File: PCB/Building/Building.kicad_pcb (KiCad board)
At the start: 2 copper layers, 57.7 x 111.5 mm, 34 parts, among them IC1 HT16K33-28SOP, IC2 HT16K33-28SOP, IC3 HT16K33-28SOP, J1 Conn_01x05, U1 OSL60362_IX, U2 OSL60362_IX, U3 OSL60362_IX, U4 OSL60362_IX, U5 OSL60362_IX, U6 OSL60362_IX

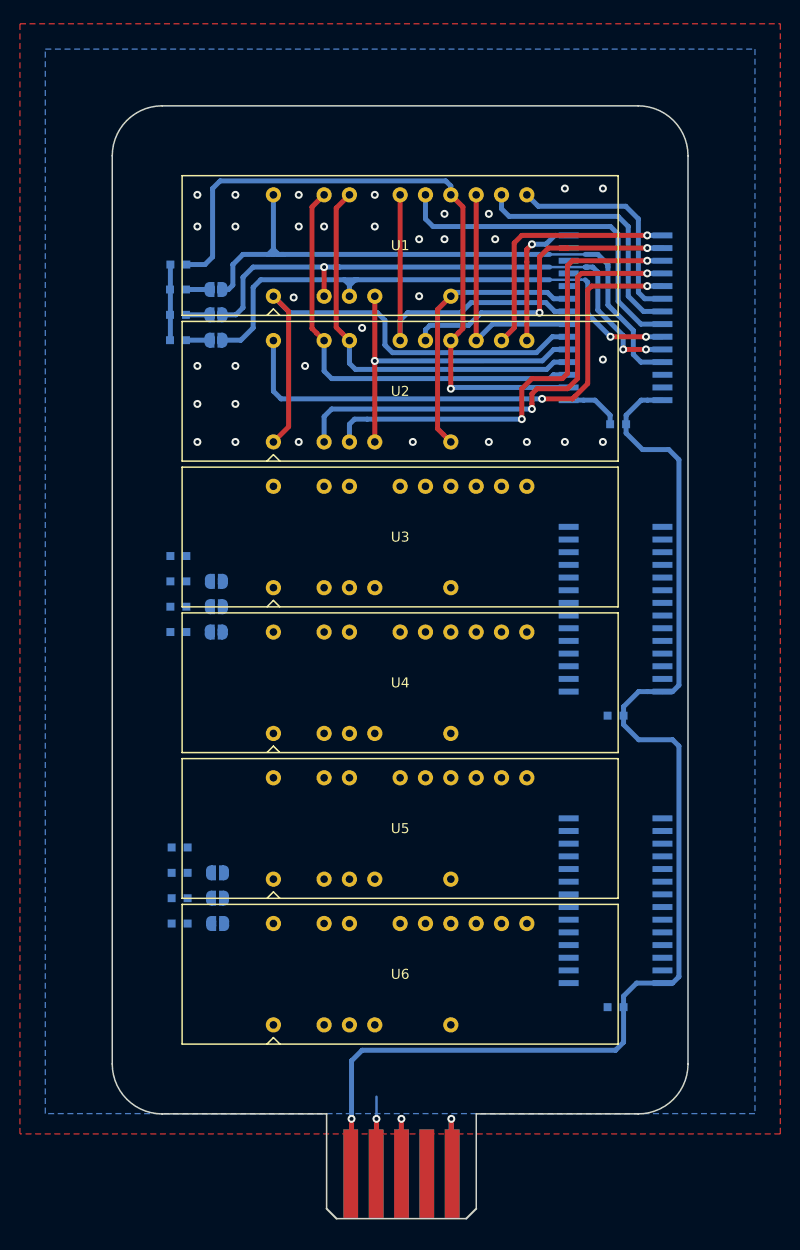
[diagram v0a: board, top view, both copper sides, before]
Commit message: (Building) 基板外形を 7mm から 8mm に拡張 #75
* HT16K33 の脇が狭すぎかつ I2C 信号を通せそうになかったため
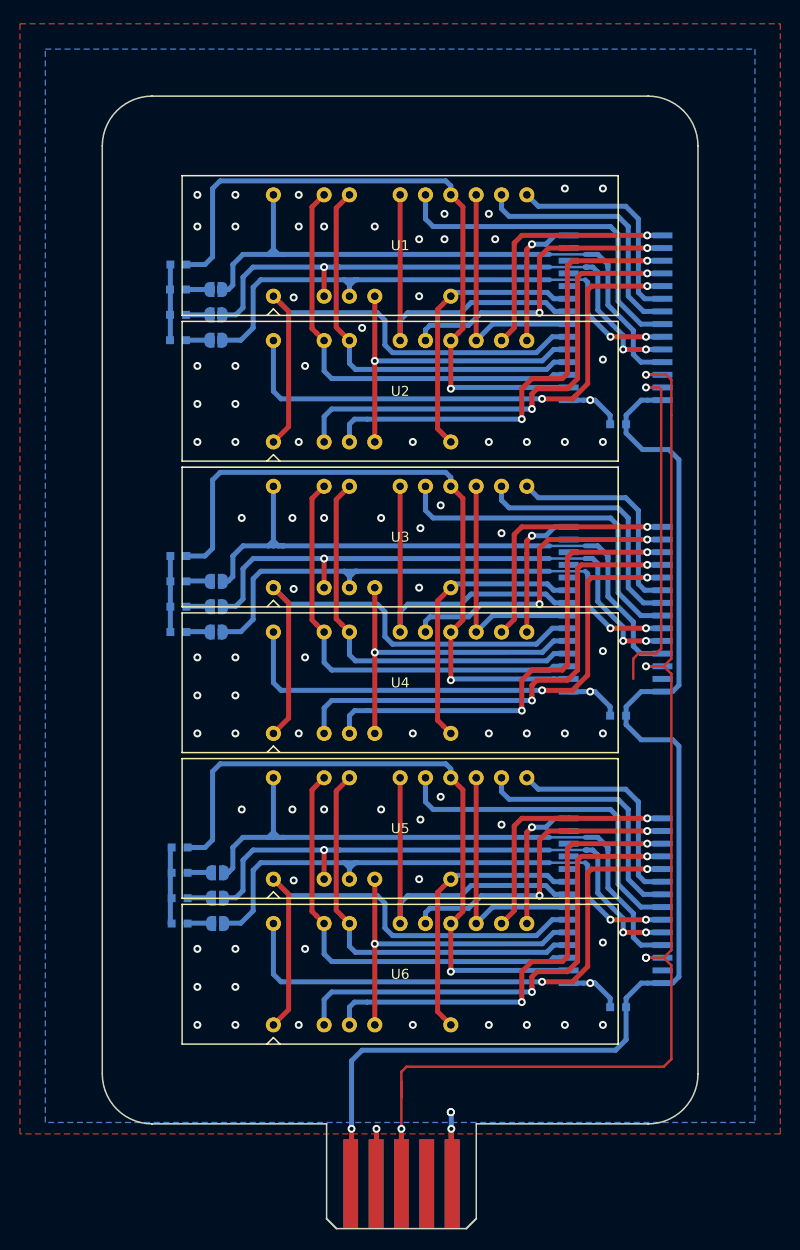
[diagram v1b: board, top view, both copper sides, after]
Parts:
- moved J1 1.00 mm to (138.2, 135.8)
- moved C2 0.25 mm to (159.9, 88.9)
- moved C3 0.25 mm to (159.9, 118.1)
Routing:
- net SCL: track 12.5 -> 129.7 mm, vias 1 -> 5
- net /A_3: track 0.00 -> 67.4 mm, vias 0 -> 1
- net /A_2: track 0.00 -> 67.4 mm, vias 0 -> 1
- net /CA25: track 0.00 -> 63.5 mm
- net /CA13: track 0.00 -> 63.5 mm
- net /CA26: track 0.00 -> 58.0 mm, vias 0 -> 3
- net /CA14: track 0.00 -> 58.0 mm, vias 0 -> 3
- net /CA27: track 0.00 -> 57.1 mm, vias 0 -> 2
- net /CA15: track 0.00 -> 57.1 mm, vias 0 -> 2
- net /CA31: track 0.00 -> 54.8 mm, vias 0 -> 2
- net /CA19: track 0.00 -> 54.8 mm, vias 0 -> 2
- net /E_2: track 0.00 -> 50.6 mm
- net /E_3: track 0.00 -> 50.6 mm
- net /CA20: track 0.00 -> 49.4 mm, vias 0 -> 2
- net /CA32: track 0.00 -> 49.4 mm, vias 0 -> 2
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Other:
- board size 57.7 x 111.5 mm -> 59.7 x 113.5 mm

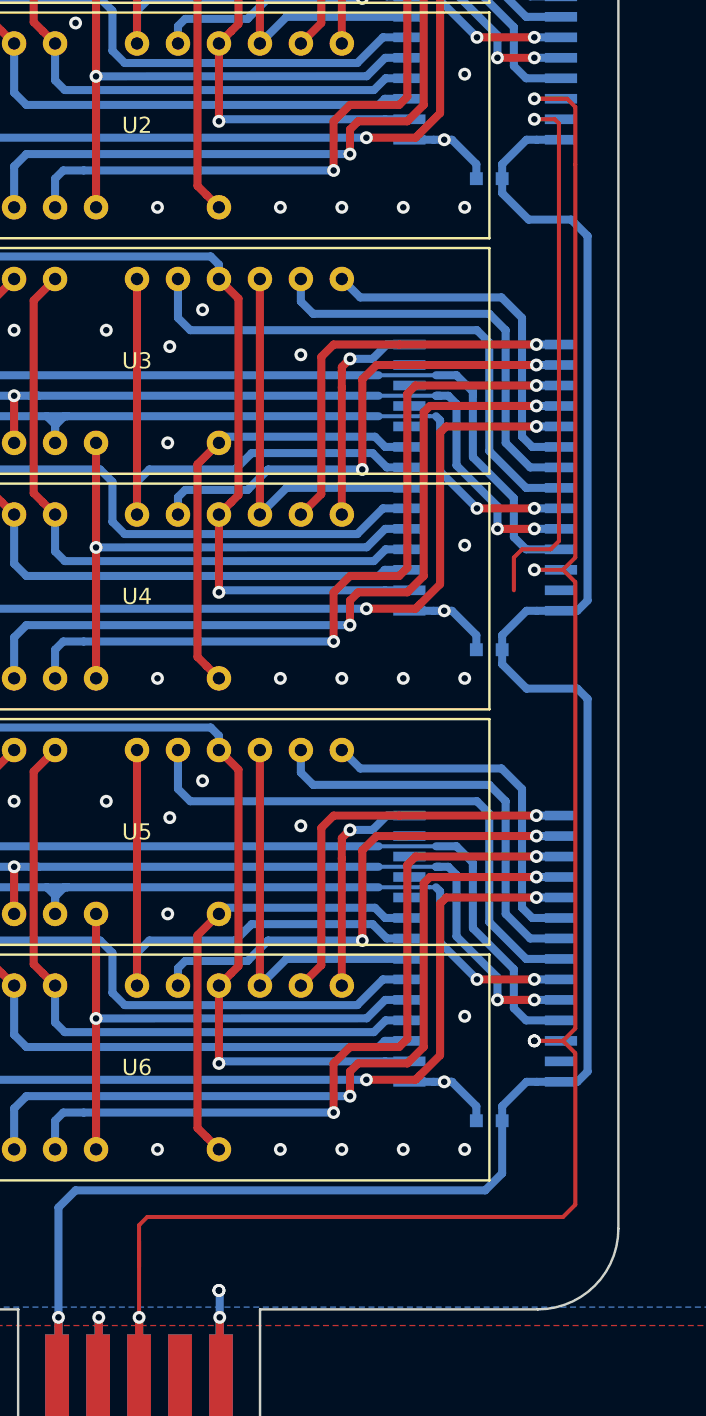
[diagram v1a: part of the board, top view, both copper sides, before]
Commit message: (Building) SCL/SDA/5V の仮配線 #75
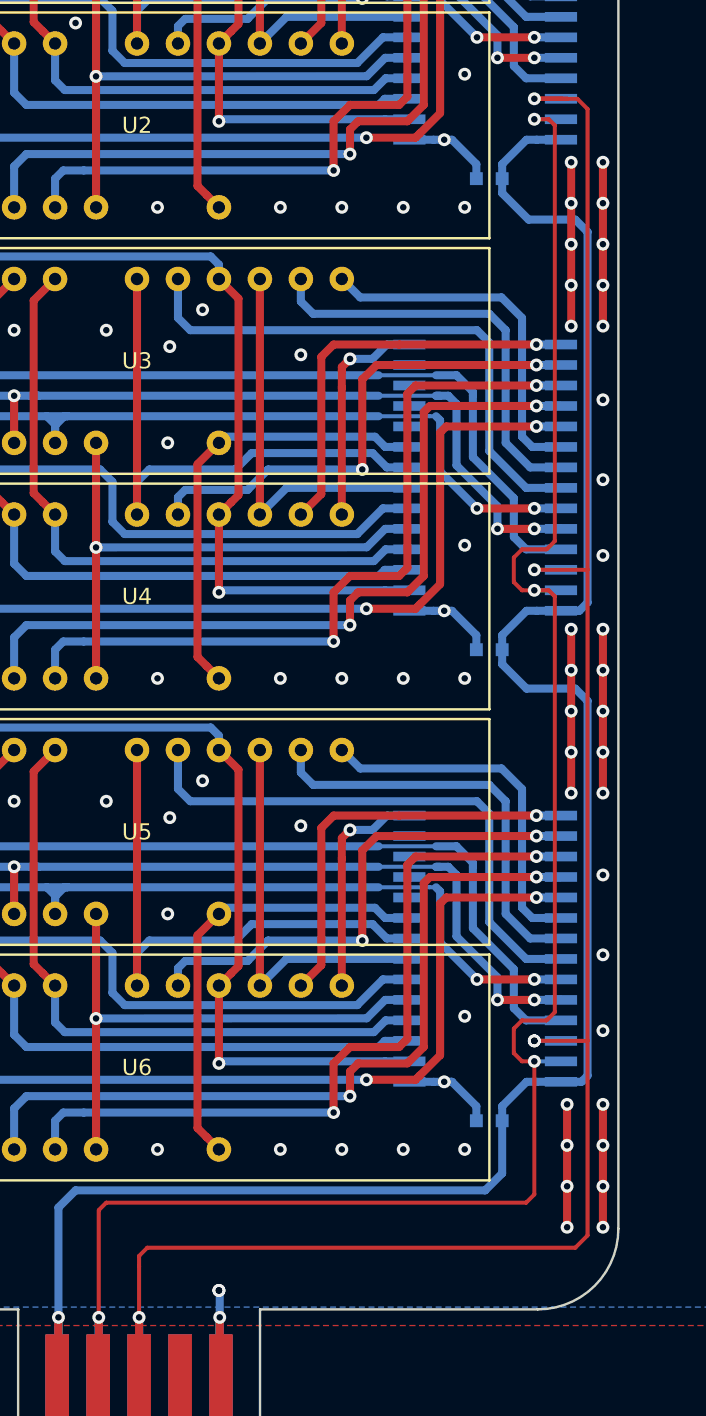
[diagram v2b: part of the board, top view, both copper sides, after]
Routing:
- net SDA: track 47.0 -> 126.2 mm, vias 2 -> 4
- net GND: track 35.0 -> 90.9 mm, vias 84 -> 118
- net SCL: track 129.7 -> 133.4 mm

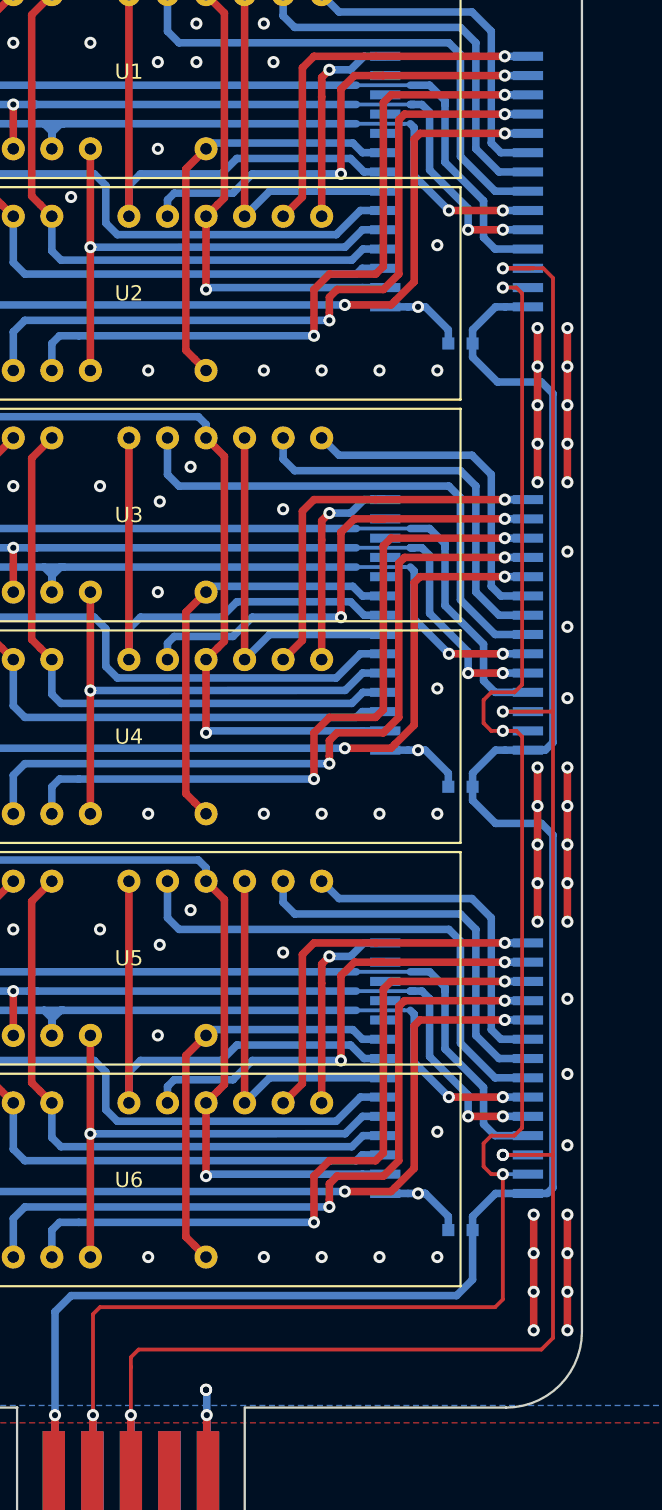
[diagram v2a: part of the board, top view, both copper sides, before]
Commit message: (Building) SCL/SDA の配線位置確定 #75
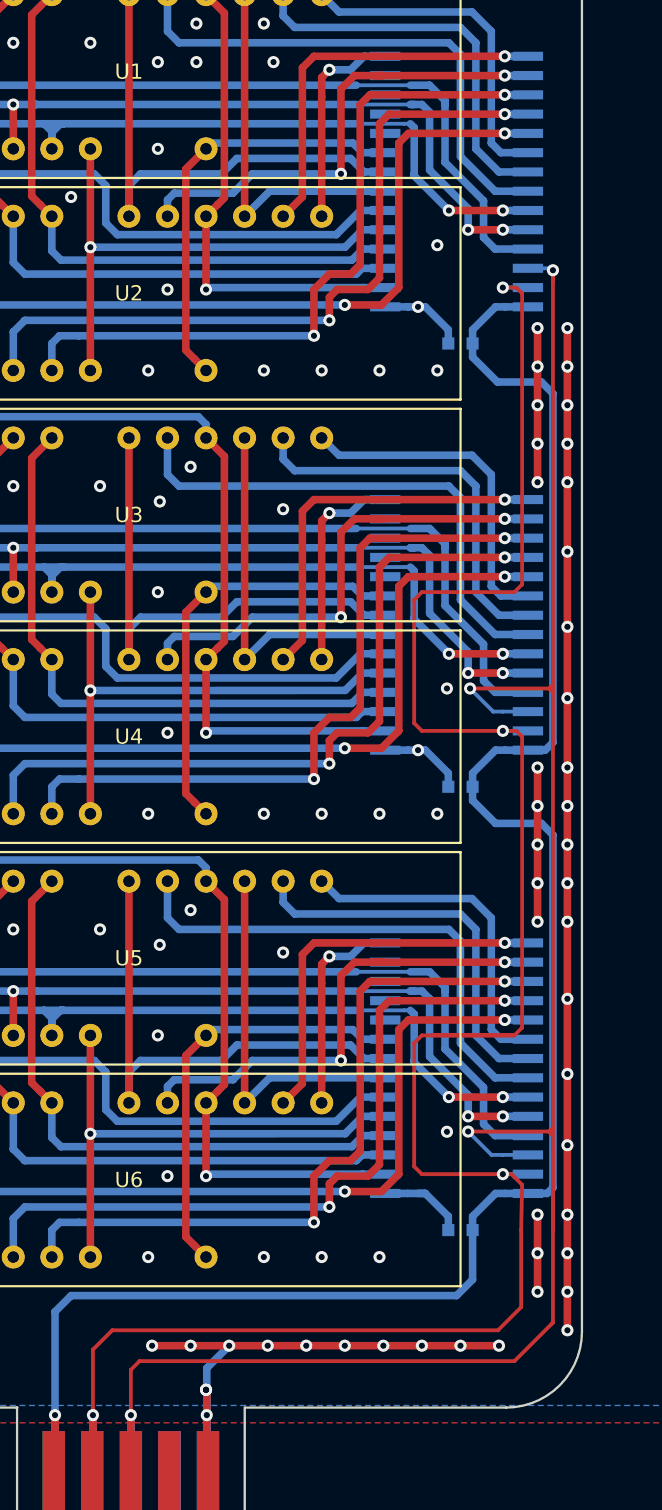
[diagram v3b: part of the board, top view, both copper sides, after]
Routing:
- net GND: track 90.9 -> 154.5 mm, vias 118 -> 128
- net SDA: track 126.2 -> 150.9 mm
- net SCL: track 133.4 -> 142.2 mm, vias 5 -> 4

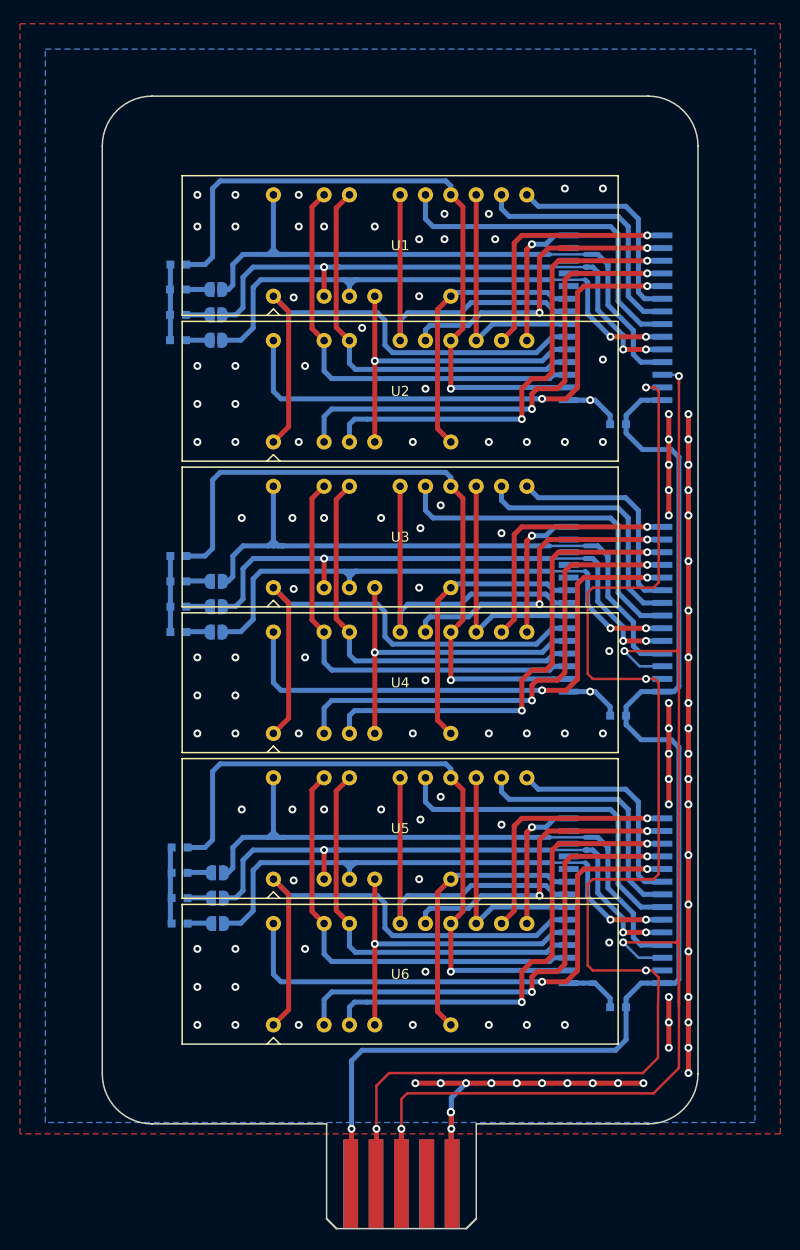
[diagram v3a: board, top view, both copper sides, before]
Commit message: (Building) 作品名シルク追加、GNDビア打ち、ティアドロップ追加 #75
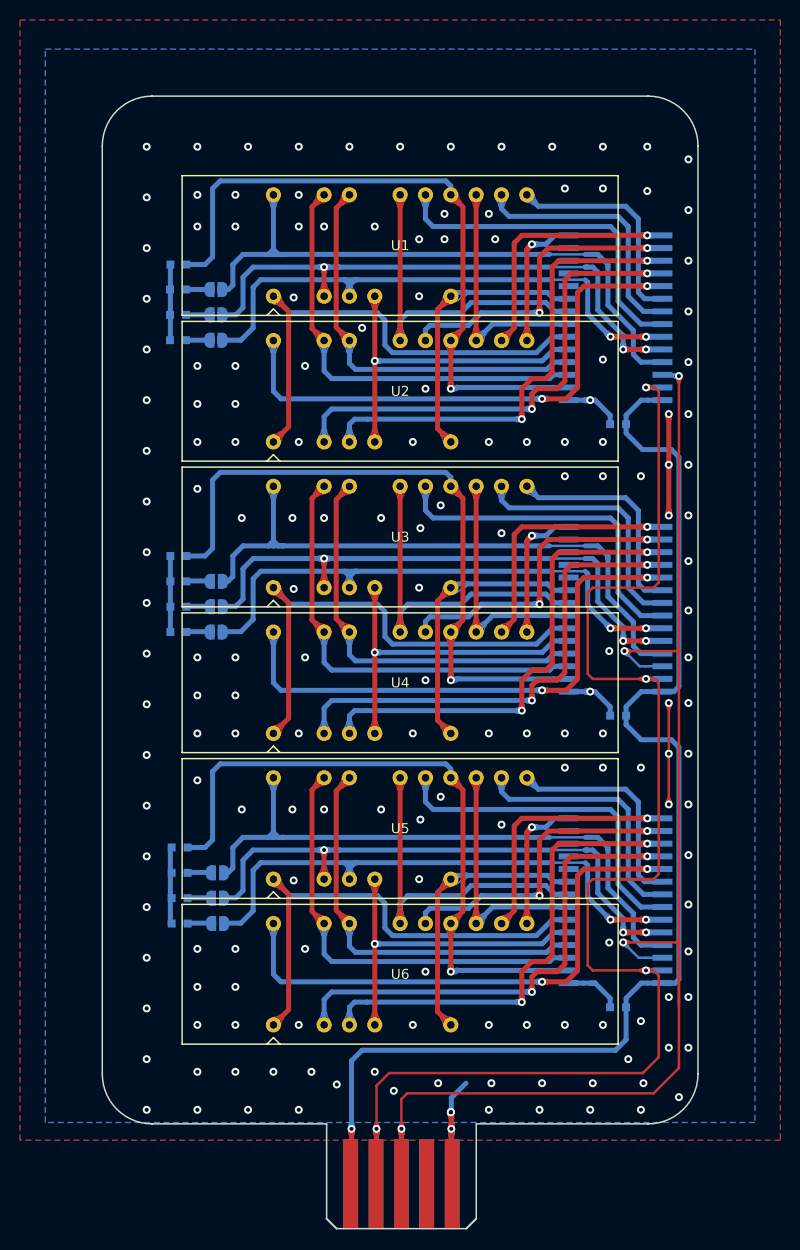
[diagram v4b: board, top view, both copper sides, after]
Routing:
- net GND: track 154.5 -> 60.5 mm, vias 128 -> 174
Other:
- board text added: "@ext_sui 2023.09"
- board text added: "The Building v1.0"
